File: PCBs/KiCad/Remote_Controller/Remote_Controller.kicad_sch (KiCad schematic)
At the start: 0 parts

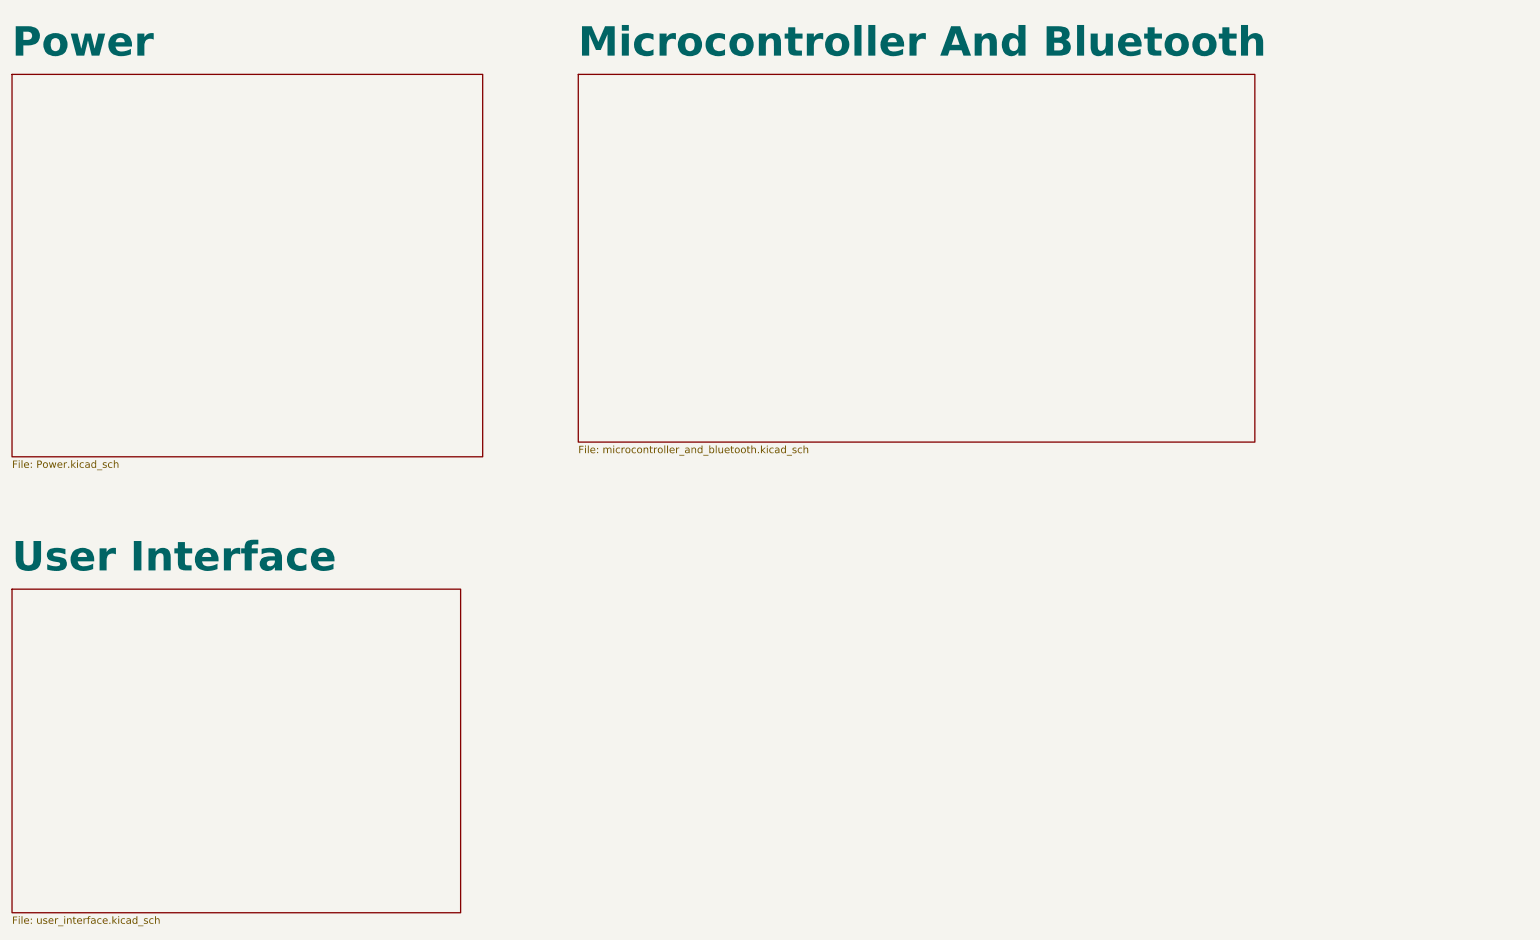
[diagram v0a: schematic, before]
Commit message: Numbered all of the schematics
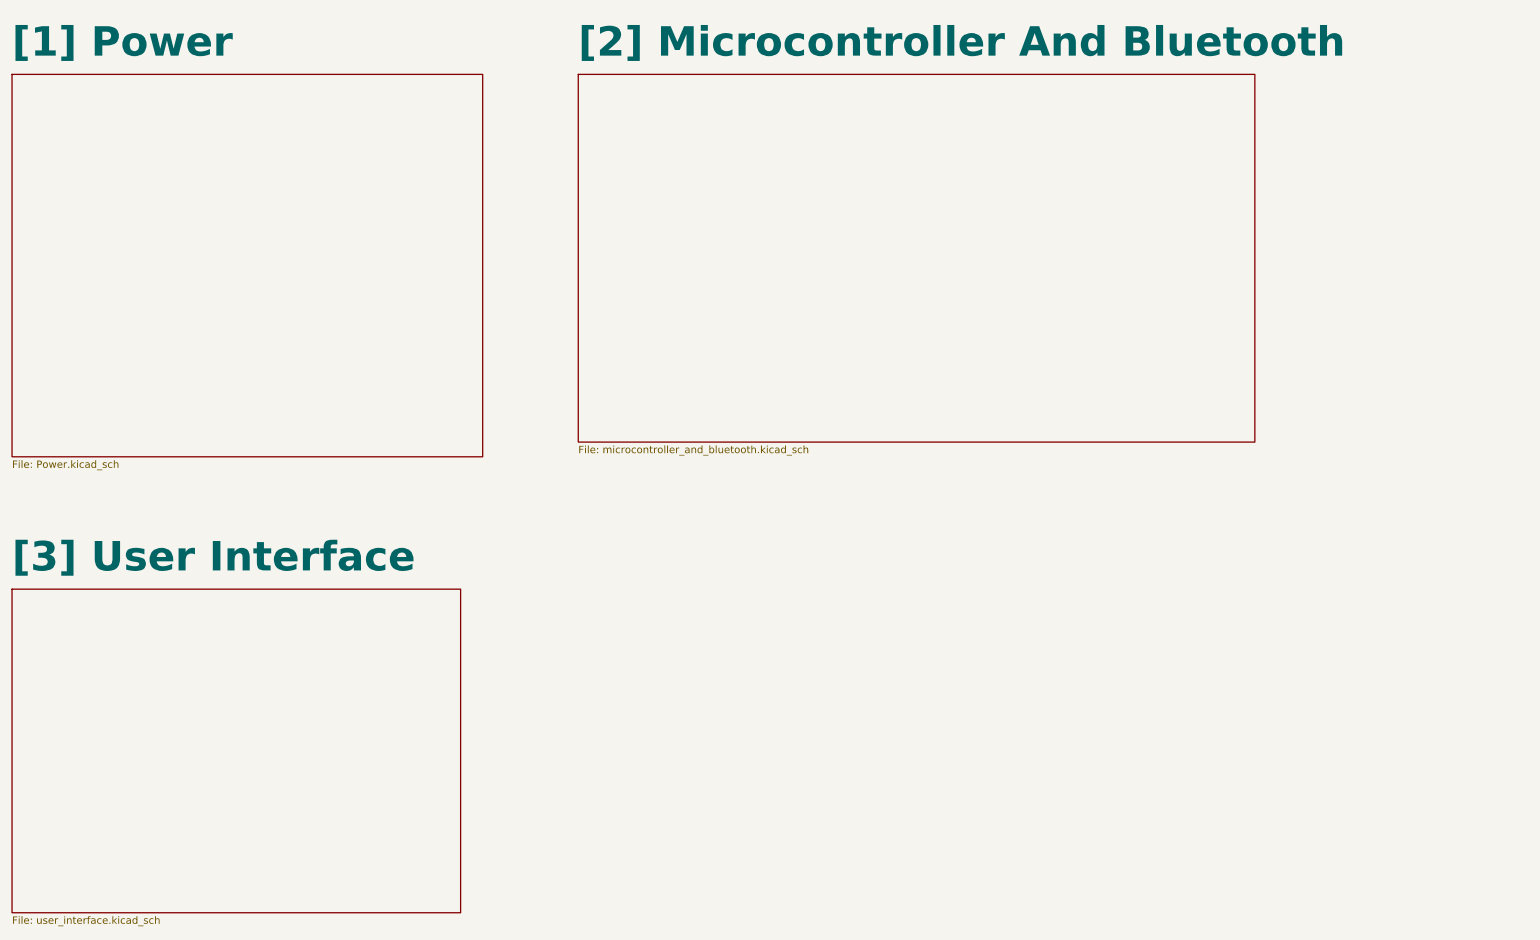
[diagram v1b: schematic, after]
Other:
- sheet Microcontroller And Bluetooth renamed [2] Microcontroller And Bluetooth
- sheet Power renamed [1] Power
- sheet User Interface renamed [3] User Interface
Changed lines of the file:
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@@
 			(color 0 0 0 0.0000)
 		)
-		(property "Sheetname" "User Interface"
+		(property "Sheetname" "[3] User Interface"
 			(at 41.91 118.0334 0)
 			(effects
@@
 			(color 0 0 0 0.0000)
 		)
-		(property "Sheetname" "Microcontroller And Bluetooth"
+		(property "Sheetname" "[2] Microcontroller And Bluetooth"
 			(at 139.7 29.1334 0)
 			(effects
@@
 			(color 0 0 0 0.0000)
 		)
-		(property "Sheetname" "Power"
+		(property "Sheetname" "[1] Power"
 			(at 41.91 29.1334 0)
 			(effects

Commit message: Added silkscreen text and made manufacturing files
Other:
- title: (none) -> SurvBot - Remote Controller
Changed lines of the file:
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@@
 	(generator_version "8.0")
 	(paper "A4")
+	(title_block
+		(title "SurvBot - Remote Controller")
+		(date "2025-03-17")
+		(rev "1.0.0.")
+	)
 	(sheet
 		(at 41.91 120.65)

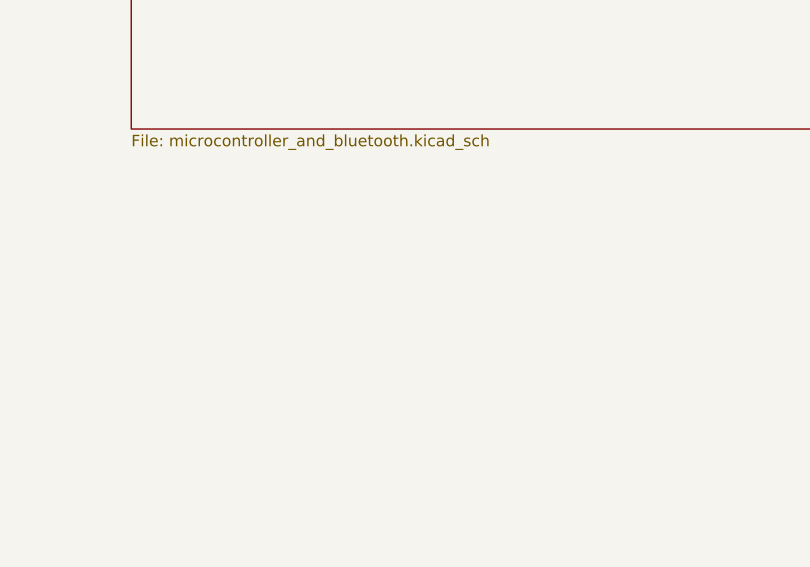
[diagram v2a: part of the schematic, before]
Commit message: Added mounting holes
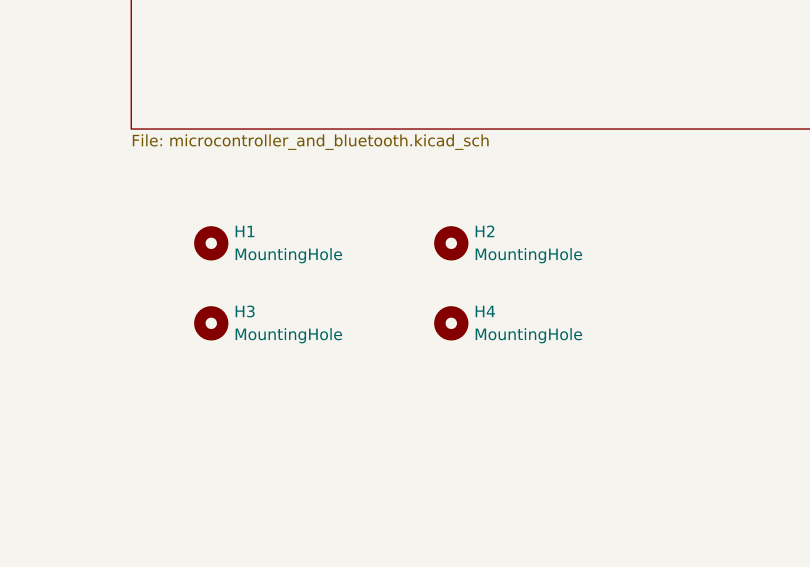
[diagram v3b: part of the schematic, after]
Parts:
- added H1, H2, H3, H4: MountingHole, MountingHole:MountingHole_2mm, symbol Mechanical:MountingHole
